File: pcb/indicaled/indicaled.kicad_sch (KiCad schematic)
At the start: 18 parts

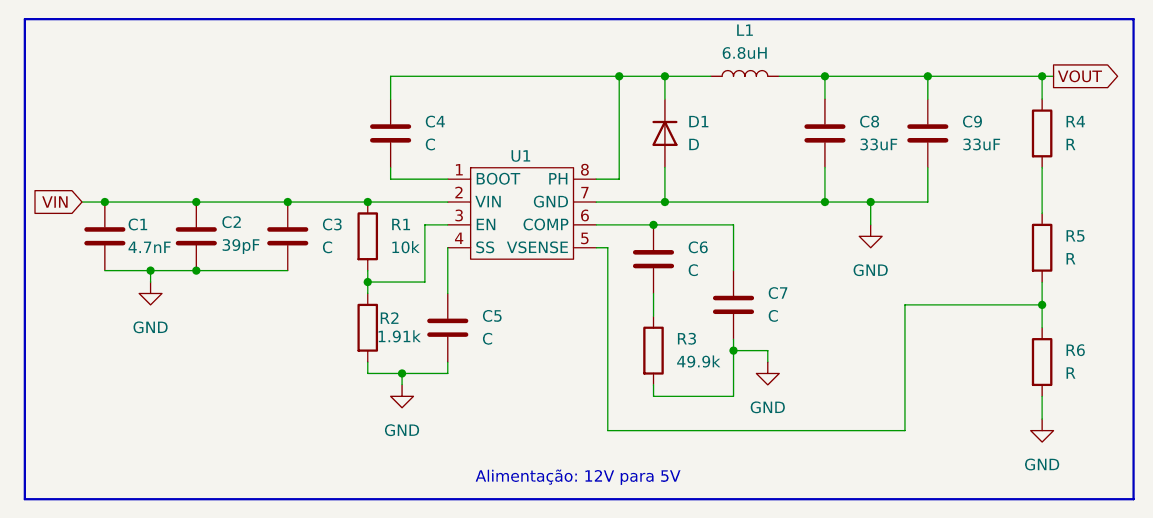
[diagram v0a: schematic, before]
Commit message: adicionando valores aos componentes
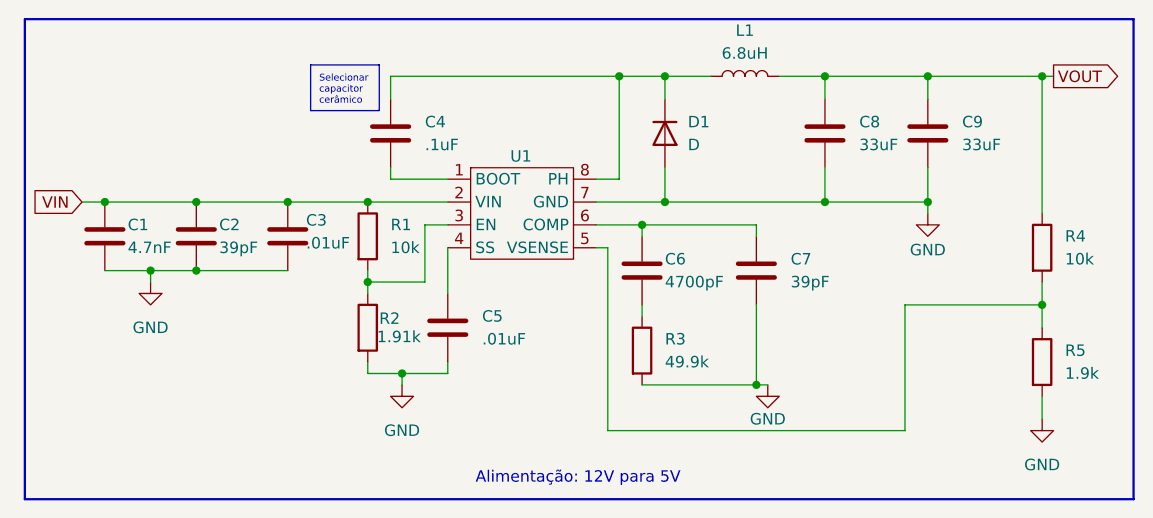
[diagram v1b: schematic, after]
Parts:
- removed R4: R, symbol Device:R
- C3, C5: value C -> .01uF
- C4: value C -> .1uF
- C6: value C -> 4700pF
- C7: value C -> 39pF
- D1: footprint (none) -> ss26:SS26
- R4: renamed from R5; value R -> 10k
- R5: renamed from R6; value R -> 1.9k
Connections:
- net VOUT: now also R4.1
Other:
- moved on the sheet: C6, C7, R3

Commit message: adicionando footprints aos componentes do circuito de alimentação
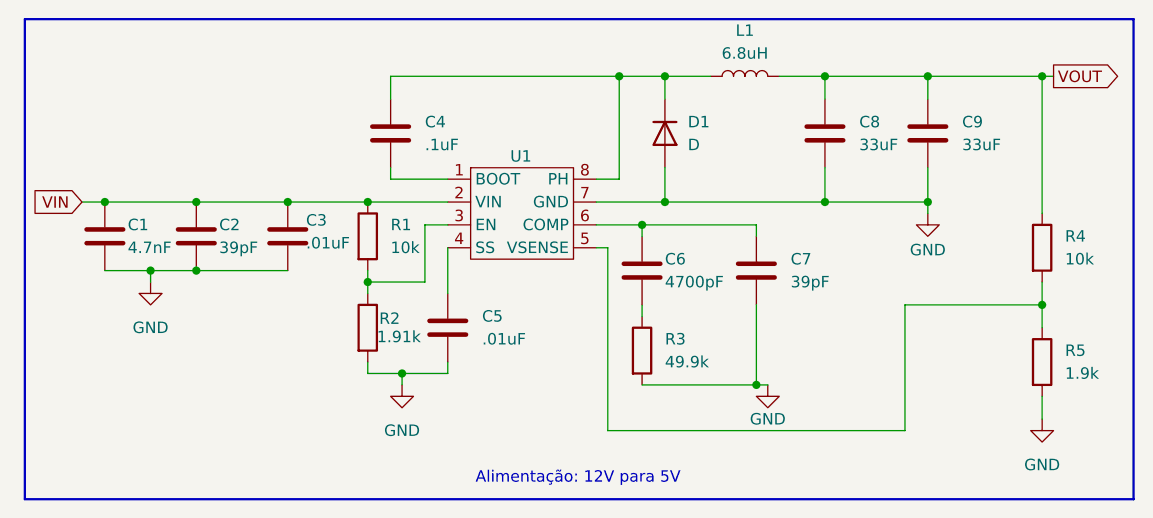
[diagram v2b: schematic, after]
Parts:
- C1, C2, C3, C4, C5: footprint (none) -> Capacitor_SMD:C_0201_0603Metric
- C6, C7: footprint (none) -> Capacitor_SMD:C_0805_2012Metric
- C8, C9: footprint (none) -> Capacitor_SMD:C_1210_3225Metric
- L1: footprint (none) -> Inductor_SMD:L_APV_ANR4020
- R1, R2, R3, R4, R5: footprint (none) -> Resistor_SMD:R_0402_1005Metric
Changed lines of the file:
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@@
-		)
-	)
-	(text_box "Selecionar capacitor cerâmico"
-		(exclude_from_sim no)
-		(at 46.99 20.32 0)
-		(size 7.62 5.08)
-		(margins 0.9525 0.9525 0.9525 0.9525)
-		(stroke
-			(width 0)
-			(type solid)
-		)
-		(fill
-			(type none)
-		)
-		(effects
-			(font
-				(size 0.762 0.762)
-			)
-			(justify left top)
 		)
 	)
@@
 			)
 		)
-		(property "Footprint" ""
+		(property "Footprint" "Resistor_SMD:R_0402_1005Metric"
 			(at 51.562 49.53 90)
 			(effects
@@
 			)
 		)
-		(property "Footprint" ""
+		(property "Footprint" "Capacitor_SMD:C_0201_0603Metric"
 			(at 63.1952 53.34 0)
 			(effects
@@
 			)
 		)
-		(property "Footprint" ""
+		(property "Footprint" "Resistor_SMD:R_0402_1005Metric"
 			(at 126.492 53.34 90)
 			(effects
@@
 			)
 		)
-		(property "Footprint" ""
+		(property "Footprint" "Capacitor_SMD:C_0201_0603Metric"
 			(at 25.0952 43.18 0)
 			(effects
@@
 			)
 		)
-		(property "Footprint" ""
+		(property "Footprint" "Inductor_SMD:L_APV_ANR4020"
 			(at 95.25 21.59 0)
 			(effects
@@
 			)
 		)
-		(property "Footprint" ""
+		(property "Footprint" "Resistor_SMD:R_0402_1005Metric"
 			(at 51.562 39.37 90)
 			(effects
@@
 			)
 		)
-		(property "Footprint" ""
+		(property "Footprint" "Capacitor_SMD:C_0805_2012Metric"
 			(at 97.4852 46.99 0)
 			(effects
@@
 		)
 		(property "Value" "~"
-			(at 70.485 30.48 0)
-			(effects
-				(font
-					(size 1.27 1.27)
-				)
+			(at 70.358 29.21 0)
+			(effects
+				(font
+					(size 1.27 1.27)
+				)
+				(hide yes)
 			)
 		)
@@
 			)
 		)
-		(property "Footprint" ""
+		(property "Footprint" "Capacitor_SMD:C_1210_3225Metric"
 			(at 105.1052 31.75 0)
 			(effects
@@
 			)
 		)
-		(property "Footprint" ""
+		(property "Footprint" "Capacitor_SMD:C_0805_2012Metric"
 			(at 84.7852 46.99 0)
 			(effects
@@
 			)
 		)
-		(property "Footprint" ""
+		(property "Footprint" "Capacitor_SMD:C_1210_3225Metric"
 			(at 116.5352 31.75 0)
 			(effects
@@
 			)
 		)
-		(property "Footprint" ""
+		(property "Footprint" "Capacitor_SMD:C_0201_0603Metric"
 			(at 45.4152 43.18 0)
 			(effects
@@
 			)
 		)
-		(property "Footprint" ""
+		(property "Footprint" "Resistor_SMD:R_0402_1005Metric"
 			(at 126.492 40.64 90)
 			(effects
@@
 			)
 		)
-		(property "Footprint" ""
+		(property "Footprint" "Capacitor_SMD:C_0201_0603Metric"
 			(at 56.8452 31.75 0)
 			(effects
@@
 			)
 		)
-		(property "Footprint" ""
+		(property "Footprint" "Resistor_SMD:R_0402_1005Metric"
 			(at 82.042 52.07 90)
 			(effects
@@
 			)
 		)
-		(property "Footprint" ""
+		(property "Footprint" "Capacitor_SMD:C_0201_0603Metric"
 			(at 35.2552 43.18 0)
 			(effects

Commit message: fazendo as ligações do circuito de alimentação e mudando o footprint do D1
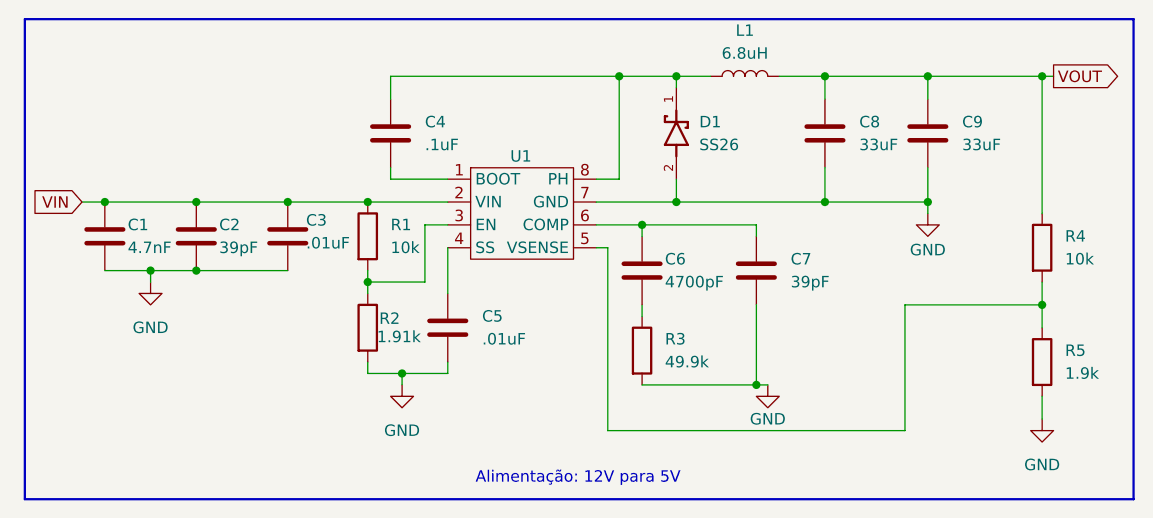
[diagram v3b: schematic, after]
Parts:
- removed D1: D, ss26:SS26, symbol Device:D
- added D1: SS26, ss26:SS26, symbol diodes:SS26
- C4: footprint Capacitor_SMD:C_0201_0603Metric -> Capacitor_SMD:C_0402_1005Metric
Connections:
- net GND: now also D1.2
- net at C4.1, L1.1, U1.8 (PH): now also D1.1
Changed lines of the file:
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@@
-	)
-	(junction
-		(at 86.36 21.59)
-		(diameter 0)
-		(color 0 0 0 0)
 	)
 	(junction
@@
 	)
 	(junction
+		(at 87.63 35.56)
+		(diameter 0)
+		(color 0 0 0 0)
+	)
+	(junction
 		(at 34.29 35.56)
 		(diameter 0)
@@
 	)
 	(junction
+		(at 87.63 21.59)
+		(diameter 0)
+		(color 0 0 0 0)
+	)
+	(junction
 		(at 81.28 21.59)
 		(diameter 0)
@@
 		(color 0 0 0 0)
 	)
-	(junction
-		(at 86.36 35.56)
-		(diameter 0)
-		(color 0 0 0 0)
+	(wire
+		(pts
+			(xy 87.63 33.02) (xy 87.63 35.56)
+		)
+		(stroke
+			(width 0)
+			(type default)
+		)
 	)
 	(wire
@@
 	(wire
 		(pts
+			(xy 87.63 21.59) (xy 87.63 22.86)
+		)
+		(stroke
+			(width 0)
+			(type default)
+		)
+	)
+	(wire
+		(pts
 			(xy 55.88 21.59) (xy 81.28 21.59)
 		)
@@
 	(wire
 		(pts
-			(xy 104.14 35.56) (xy 86.36 35.56)
+			(xy 78.74 35.56) (xy 87.63 35.56)
 		)
 		(stroke
@@
 	(wire
 		(pts
-			(xy 86.36 35.56) (xy 86.36 31.75)
-		)
-		(stroke
-			(width 0)
-			(type default)
-		)
-	)
-	(wire
-		(pts
 			(xy 55.88 33.02) (xy 62.23 33.02)
 		)
@@
 	(wire
 		(pts
-			(xy 78.74 35.56) (xy 86.36 35.56)
-		)
-		(stroke
-			(width 0)
-			(type default)
-		)
-	)
-	(wire
-		(pts
 			(xy 80.01 60.96) (xy 80.01 40.64)
 		)
@@
 	(wire
 		(pts
-			(xy 81.28 21.59) (xy 86.36 21.59)
-		)
-		(stroke
-			(width 0)
-			(type default)
-		)
-	)
-	(wire
-		(pts
-			(xy 86.36 21.59) (xy 86.36 24.13)
-		)
-		(stroke
-			(width 0)
-			(type default)
-		)
-	)
-	(wire
-		(pts
-			(xy 86.36 21.59) (xy 91.44 21.59)
+			(xy 81.28 21.59) (xy 87.63 21.59)
 		)
 		(stroke
@@
 	(wire
 		(pts
+			(xy 87.63 21.59) (xy 91.44 21.59)
+		)
+		(stroke
+			(width 0)
+			(type default)
+		)
+	)
+	(wire
+		(pts
 			(xy 29.21 43.18) (xy 29.21 44.45)
 		)
@@
 		(pts
 			(xy 128.27 46.99) (xy 128.27 49.53)
+		)
+		(stroke
+			(width 0)
+			(type default)
+		)
+	)
+	(wire
+		(pts
+			(xy 87.63 35.56) (xy 104.14 35.56)
 		)
 		(stroke
@@
 	)
 	(symbol
-		(lib_id "Device:D")
-		(at 86.36 27.94 270)
-		(unit 1)
-		(exclude_from_sim no)
-		(in_bom yes)
-		(on_board yes)
-		(dnp no)
-		(fields_autoplaced yes)
-		(property "Reference" "D1"
-			(at 88.9 26.6699 90)
-			(effects
-				(font
-					(size 1.27 1.27)
-				)
-				(justify left)
-			)
-		)
-		(property "Value" "D"
-			(at 88.9 29.2099 90)
-			(effects
-				(font
-					(size 1.27 1.27)
-				)
-				(justify left)
-			)
-		)
-		(property "Footprint" "ss26:SS26"
-			(at 86.36 27.94 0)
-			(effects
-				(font
-					(size 1.27 1.27)
-				)
-				(hide yes)
-			)
-		)
-		(property "Datasheet" "~"
-			(at 86.36 27.94 0)
-			(effects
-				(font
-					(size 1.27 1.27)
-				)
-				(hide yes)
-			)
-		)
-		(property "Description" "Diode"
-			(at 86.36 27.94 0)
-			(effects
-				(font
-					(size 1.27 1.27)
-				)
-				(hide yes)
-			)
-		)
-		(property "Sim.Device" "D"
-			(at 86.36 27.94 0)
-			(effects
-				(font
-					(size 1.27 1.27)
-				)
-				(hide yes)
-			)
-		)
-		(property "Sim.Pins" "1=K 2=A"
-			(at 86.36 27.94 0)
-			(effects
-				(font
-					(size 1.27 1.27)
-				)
-				(hide yes)
-			)
-		)
-		(pin "1"
-		)
-		(pin "2"
-		)
-		(instances
-			(project ""
-				(path "/8b90307c-355e-4020-9754-332457e33a11"
-					(reference "D1")
-					(unit 1)
-				)
-			)
-		)
-	)
-	(symbol
 		(lib_id "Device:L")
 		(at 95.25 21.59 90)
@@
 	)
 	(symbol
+		(lib_id "diodes:SS26")
+		(at 87.63 27.94 90)
+		(unit 1)
+		(exclude_from_sim no)
+		(in_bom yes)
+		(on_board yes)
+		(dnp no)
+		(fields_autoplaced yes)
+		(property "Reference" "D1"
+			(at 90.17 26.6699 90)
+			(effects
+				(font
+					(size 1.27 1.27)
+				)
+				(justify right)
+			)
+		)
+		(property "Value" "SS26"
+			(at 90.17 29.2099 90)
+			(effects
+				(font
+					(size 1.27 1.27)
+				)
+				(justify right)
+			)
+		)
+		(property "Footprint" "ss26:SS26"
+			(at 93.472 28.194 0)
+			(effects
+				(font
+					(size 1.27 1.27)
+				)
+				(justify bottom)
+				(hide yes)
+			)
+		)
+		(property "Datasheet" ""
+			(at 87.63 27.94 0)
+			(effects
+				(font
+					(size 1.27 1.27)
+				)
+				(hide yes)
+			)
+		)
+		(property "Description" ""
+			(at 87.63 27.94 0)
+			(effects
+				(font
+					(size 1.27 1.27)
+				)
+				(hide yes)
+			)
+		)
+		(property "PARTREV" "N2306"
+			(at 98.806 27.94 0)
+			(effects
+				(font
+					(size 1.27 1.27)
+				)
+				(justify bottom)
+				(hide yes)
+			)
+		)
+		(property "MANUFACTURER" "Taiwan Semiconductor"
+			(at 94.996 28.448 0)
+			(effects
+				(font
+					(size 1.27 1.27)
+				)
+				(justify bottom)
+				(hide yes)
+			)
+		)
+		(property "SNAPEDA_PN" "SS22"
+			(at 102.616 27.94 0)
+			(effects
+				(font
+					(size 1.27 1.27)
+				)
+				(justify bottom)
+				(hide yes)
+			)
+		)
+		(property "MAXIMUM_PACKAGE_HEIGHT" "2.65mm"
+			(at 100.584 27.686 0)
+			(effects
+				(font
+					(size 1.27 1.27)
+				)
+				(justify bottom)
+				(hide yes)
+			)
+		)
+		(property "STANDARD" "Manufacturer Recommendations"
+			(at 96.774 27.94 0)
+			(effects
+				(font
+					(size 1.27 1.27)
+				)
+				(justify bottom)
+				(hide yes)
+			)
+		)
+		(pin "2"
+		)
+		(pin "1"
+		)
+		(instances
+			(project ""
+				(path "/8b90307c-355e-4020-9754-332457e33a11"
+					(reference "D1")
+					(unit 1)
+				)
+			)
+		)
+	)
+	(symbol
 		(lib_id "Device:C")
 		(at 96.52 43.18 0)
@@
 			)
 		)
-		(property "Footprint" "Capacitor_SMD:C_0201_0603Metric"
+		(property "Footprint" "Capacitor_SMD:C_0402_1005Metric"
 			(at 56.8452 31.75 0)
 			(effects

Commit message: trocando os capacitores de acoplamento de 0201 para 1210
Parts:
- C1, C2, C3: footprint Capacitor_SMD:C_0201_0603Metric -> Capacitor_SMD:C_1210_3225Metric
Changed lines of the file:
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@@
 			)
 		)
-		(property "Footprint" "Capacitor_SMD:C_0201_0603Metric"
+		(property "Footprint" "Capacitor_SMD:C_1210_3225Metric"
 			(at 25.0952 43.18 0)
 			(effects
@@
 			)
 		)
-		(property "Footprint" "Capacitor_SMD:C_0201_0603Metric"
+		(property "Footprint" "Capacitor_SMD:C_1210_3225Metric"
 			(at 45.4152 43.18 0)
 			(effects
@@
 			)
 		)
-		(property "Footprint" "Capacitor_SMD:C_0201_0603Metric"
+		(property "Footprint" "Capacitor_SMD:C_1210_3225Metric"
 			(at 35.2552 43.18 0)
 			(effects

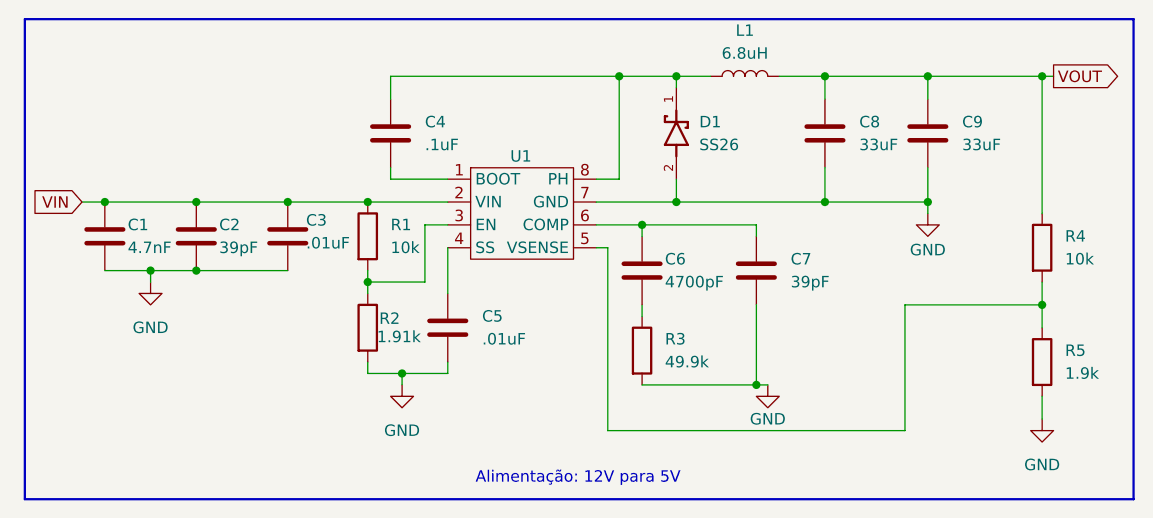
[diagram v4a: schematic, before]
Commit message: colocando o datasheet da JLCPCB nos Cins e no TPS54331
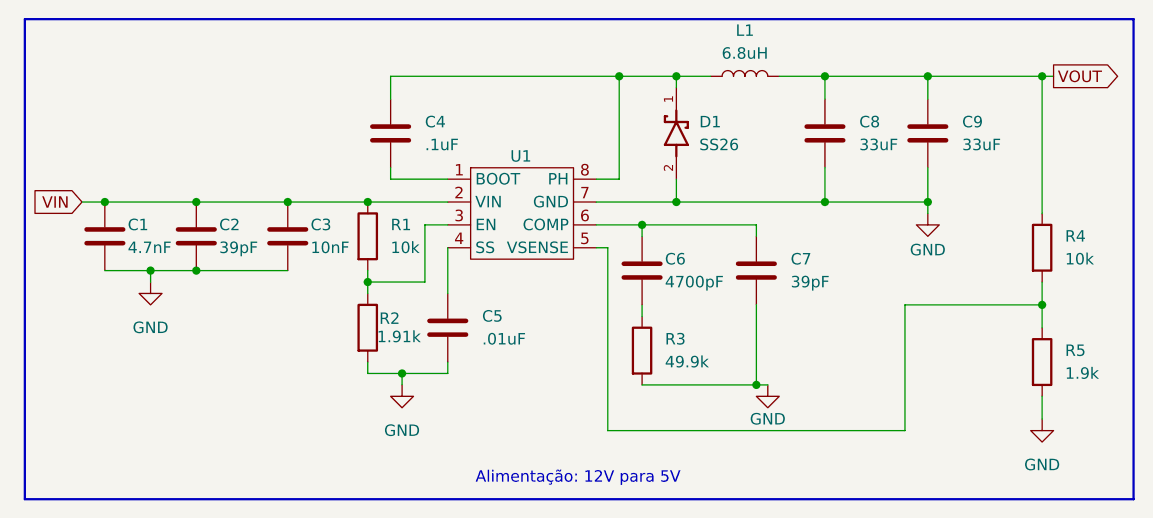
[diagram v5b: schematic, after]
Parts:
- C3: value .01uF -> 10nF
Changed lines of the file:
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@@
 			)
 		)
-		(property "Datasheet" "~"
+		(property "Datasheet" "https://jlcpcb.com/partdetail/YAGEO-CC1210JKNPO9BN472/C577266"
 			(at 24.13 39.37 0)
 			(effects
@@
 			)
 		)
-		(property "Datasheet" "https://jlcpcb.com/api/file/downloadByFileSystemAccessId/8579708378375393280"
+		(property "Datasheet" "https://jlcpcb.com/partdetail/TexasInstruments-TPS54331DR/C9865"
 			(at 68.58 33.02 0)
 			(effects
@@
 		(dnp no)
 		(property "Reference" "C3"
-			(at 46.482 37.592 0)
-			(effects
-				(font
-					(size 1.27 1.27)
-				)
-				(justify left)
-			)
-		)
-		(property "Value" ".01uF"
-			(at 46.482 40.132 0)
+			(at 46.99 38.1 0)
+			(effects
+				(font
+					(size 1.27 1.27)
+				)
+				(justify left)
+			)
+		)
+		(property "Value" "10nF"
+			(at 46.99 40.64 0)
 			(effects
 				(font
@@
 			)
 		)
-		(property "Datasheet" "~"
+		(property "Datasheet" "https://jlcpcb.com/partdetail/YAGEO-CC1210KKX7R0BB103/C527374"
 			(at 44.45 39.37 0)
 			(effects
@@
 			)
 		)
-		(property "Datasheet" "~"
+		(property "Datasheet" "https://jlcpcb.com/partdetail/KEMET-C1210C390K3HAC7800/C2209308"
 			(at 34.29 39.37 0)
 			(effects

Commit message: trocando o S26 por S24, adicionando alguns datasheets e reposicionando os componentes na PCB
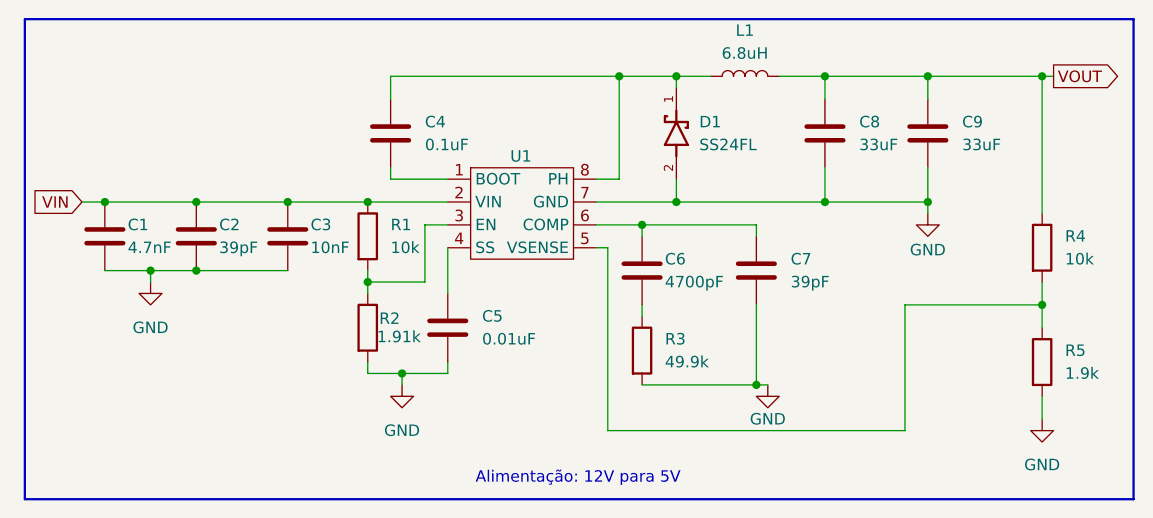
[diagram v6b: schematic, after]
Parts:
- C4: value .1uF -> 0.1uF
- C5: value .01uF -> 0.01uF
- D1: value SS26 -> SS24FL
- L1: footprint Inductor_SMD:L_APV_ANR4020 -> Inductor_SMD:L_APV_ANR5040
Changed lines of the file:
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@@
 			)
 		)
-		(property "Value" ".01uF"
+		(property "Value" "0.01uF"
 			(at 66.04 50.7999 0)
 			(effects
@@
 			)
 		)
-		(property "Footprint" "Inductor_SMD:L_APV_ANR4020"
+		(property "Footprint" "Inductor_SMD:L_APV_ANR5040"
 			(at 95.25 21.59 0)
 			(effects
@@
 			)
 		)
-		(property "Datasheet" "~"
+		(property "Datasheet" "https://jlcpcb.com/partdetail/Sunlord-SWPA5040S6R8MT/C36411"
 			(at 95.25 21.59 0)
 			(effects
@@
 			)
 		)
-		(property "Value" "SS26"
+		(property "Value" "SS24FL"
 			(at 90.17 29.2099 90)
 			(effects
@@
 			)
 		)
-		(property "Datasheet" ""
+		(property "Datasheet" "https://jlcpcb.com/partdetail/onsemi-SS24FL/C894433"
 			(at 87.63 27.94 0)
 			(effects
@@
 			)
 		)
-		(property "Value" ".1uF"
+		(property "Value" "0.1uF"
 			(at 59.69 29.2099 0)
 			(effects
@@
 			)
 		)
-		(property "Datasheet" "~"
+		(property "Datasheet" "https://jlcpcb.com/partdetail/MurataElectronics-GRM155R71A104KA01D/C71687"
 			(at 55.88 27.94 0)
 			(effects

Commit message: modificando o capacitor do pino SS
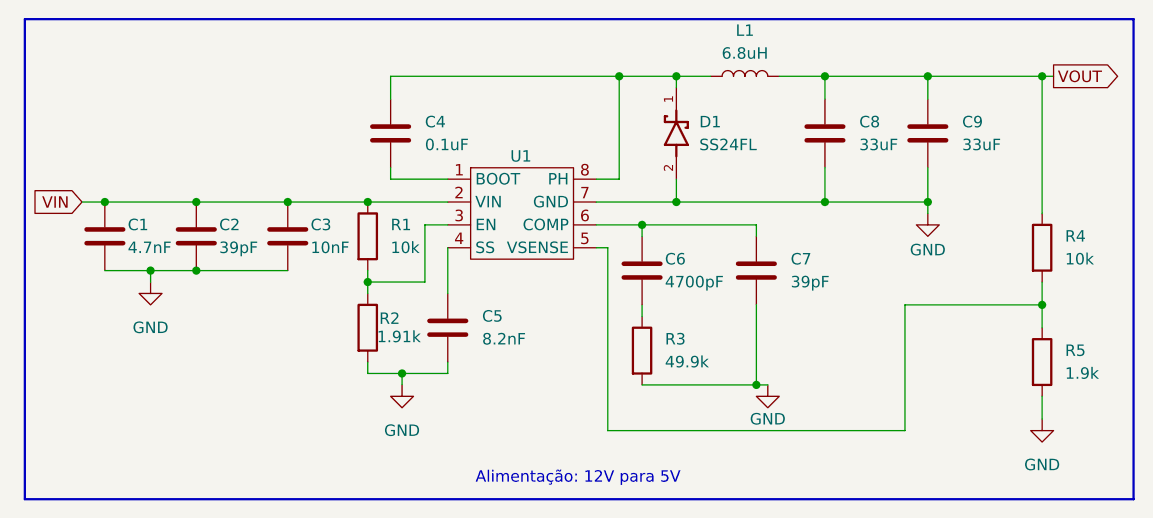
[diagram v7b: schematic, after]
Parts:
- C5: value 0.01uF -> 8.2nF
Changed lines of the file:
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@@
 			)
 		)
-		(property "Value" "0.01uF"
+		(property "Value" "8.2nF"
 			(at 66.04 50.7999 0)
 			(effects
@@
 			)
 		)
-		(property "Datasheet" "~"
+		(property "Datasheet" "https://jlcpcb.com/partdetail/2260156-GRM033R71A822KA01D/C2168104"
 			(at 62.23 49.53 0)
 			(effects
@@
 			)
 		)
-		(property "Datasheet" "https://jlcpcb.com/partdetail/TexasInstruments-TPS54331DR/C9865"
+		(property "Datasheet" "https://jlcpcb.com/api/file/downloadByFileSystemAccessId/8579708378375393280"
 			(at 68.58 33.02 0)
 			(effects
